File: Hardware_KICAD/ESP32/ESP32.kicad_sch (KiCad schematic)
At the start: 4 parts, among them U1 ESP32-S3-WROOM-1

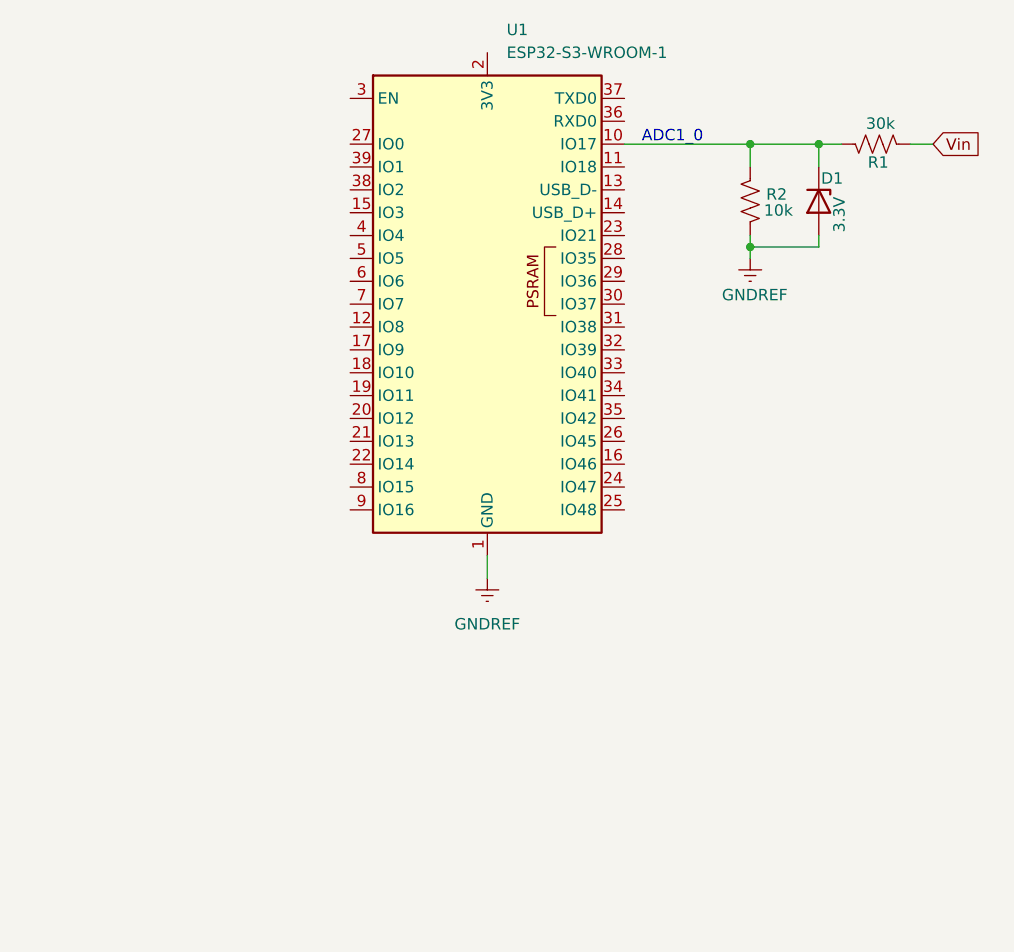
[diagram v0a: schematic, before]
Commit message: Added ProjInfo Transmit -nottetsted
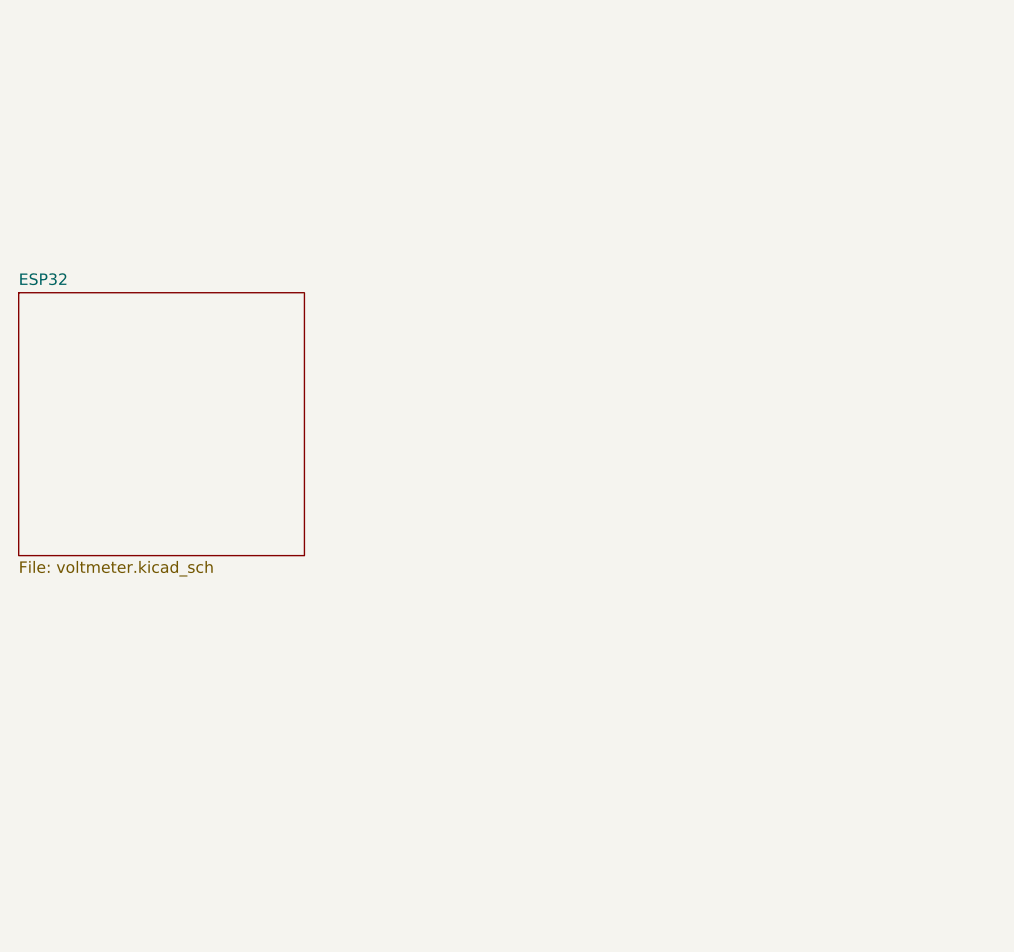
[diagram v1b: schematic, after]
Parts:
- removed D1: 3.3V, symbol Device:D_Zener
- removed R1: 30k, symbol Device:R_US
- removed R2: 10k, symbol Device:R_US
- removed U1: ESP32-S3-WROOM-1, RF_Module:ESP32-S3-WROOM-1, symbol RF_Module:ESP32-S3-WROOM-1
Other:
- added sheet ESP32 (voltmeter.kicad_sch)
- note removed: "ADC1_0"

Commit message: Added Pi and Power Schematic
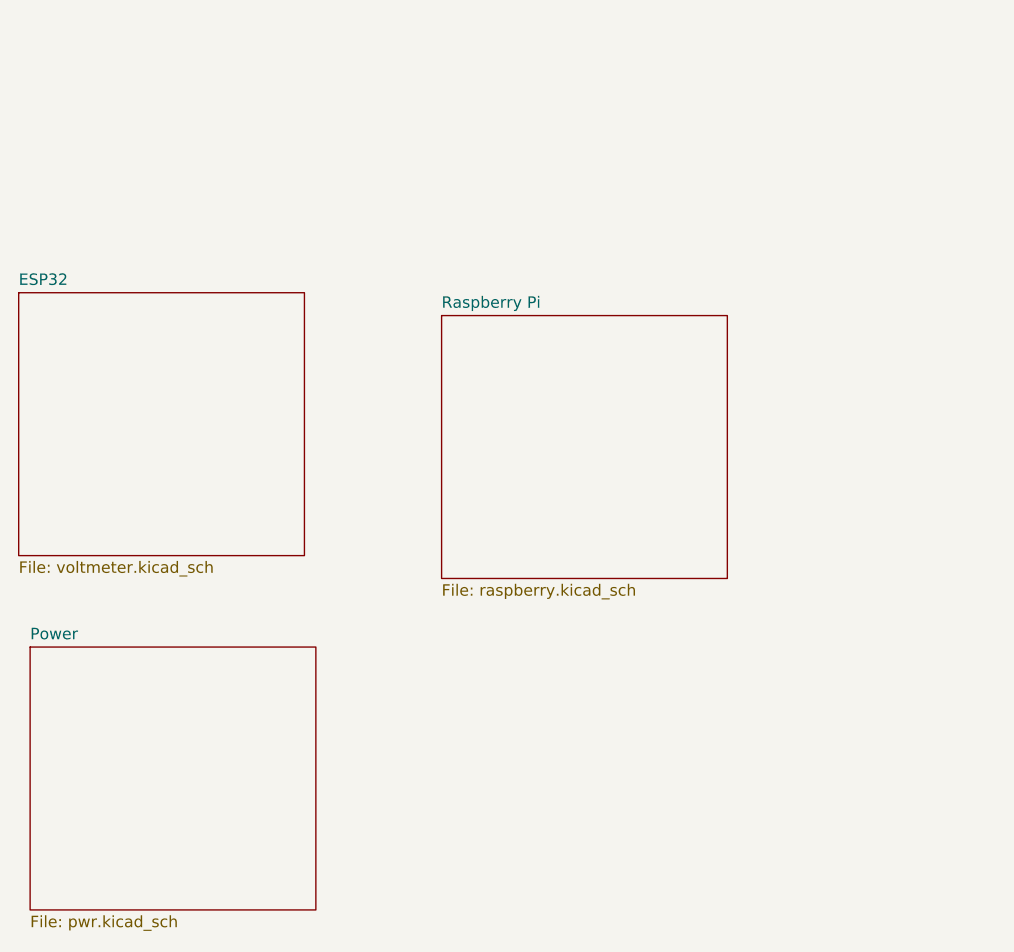
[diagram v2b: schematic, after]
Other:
- added sheet Power (pwr.kicad_sch)
- added sheet Raspberry Pi (raspberry.kicad_sch)
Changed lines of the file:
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@@
+		)
+	)
+	(sheet
+		(at 88.9 59.69)
+		(size 31.75 29.21)
+		(exclude_from_sim no)
+		(in_bom yes)
+		(on_board yes)
+		(dnp no)
+		(fields_autoplaced yes)
+		(stroke
+			(width 0.1524)
+			(type solid)
+		)
+		(fill
+			(color 255 248 130 1.0000)
+		)
+		(property "Sheetname" "Raspberry Pi"
+			(at 88.9 58.9784 0)
+			(effects
+				(font
+					(size 1.27 1.27)
+				)
+				(justify left bottom)
+			)
+		)
+		(property "Sheetfile" "raspberry.kicad_sch"
+			(at 88.9 89.4846 0)
+			(effects
+				(font
+					(size 1.27 1.27)
+				)
+				(justify left top)
+			)
+		)
+		(instances
+			(project "ESP32"
+				(path "/fc2c29e6-a963-4328-805d-ffb2dd9b9662"
+					(page "3")
+				)
+			)
+		)
+	)
+	(sheet
+		(at 43.18 96.52)
+		(size 31.75 29.21)
+		(exclude_from_sim no)
+		(in_bom yes)
+		(on_board yes)
+		(dnp no)
+		(fields_autoplaced yes)
+		(stroke
+			(width 0.1524)
+			(type solid)
+		)
+		(fill
+			(color 255 248 130 1.0000)
+		)
+		(property "Sheetname" "Power"
+			(at 43.18 95.8084 0)
+			(effects
+				(font
+					(size 1.27 1.27)
+				)
+				(justify left bottom)
+			)
+		)
+		(property "Sheetfile" "pwr.kicad_sch"
+			(at 43.18 126.3146 0)
+			(effects
+				(font
+					(size 1.27 1.27)
+				)
+				(justify left top)
+			)
+		)
+		(instances
+			(project "ESP32"
+				(path "/fc2c29e6-a963-4328-805d-ffb2dd9b9662"
+					(page "4")
+				)
+			)
 		)
 	)
